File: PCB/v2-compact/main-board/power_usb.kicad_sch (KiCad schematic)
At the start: 0 parts

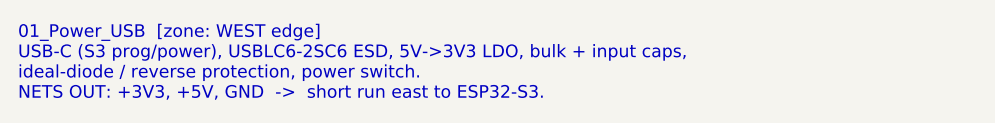
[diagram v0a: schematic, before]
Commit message: PCB: rework main board to phone-style layout; J1 -> horizontal strip
Main board (per feedback) is now a phone-style split — front is pure UI, back
carries the electronics:
- FRONT: status LEDs at the very top (above the display), TFT rotated to
  LANDSCAPE (sideways), nav buttons below it and moved down. Same feel as the
  ESP32-DIV, sideways screen.
- BACK: ESP32-S3 behind the display, microSD beside it, power + USB-C at the
  bottom-centre edge like a phone.

To keep the centre column free for the landscape display and the bottom-centre
USB-C, J1 is reoriented from a vertical 2x10 to a HORIZONTAL 10x2 strip in the
lower-centre. J1 is the shared mating datum, so the shield's J1 moves to match;
the shield's RV1106 / HTRC110 / bulk-cap zones shift to sit above/below the new
strip (SPI spine still runs north from it). Every v1 capability unchanged.

Updated both .kicad_pcb, both floorplan SVGs, both schematics' zone specs, and
PLACEMENT.md. Verified: files parse, J1 clears all zones, no same-side overlaps.

Co-Authored-By: Claude <noreply@anthropic.com>
Claude-Session: https://claude.ai/code/session_017BEAKBRVwbUCc7Sa2o3Ye7
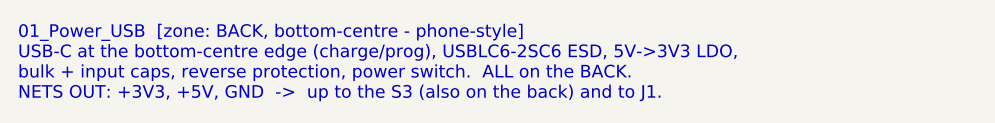
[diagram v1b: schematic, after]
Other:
- note added: "01_Power_USB [zone: BACK, bottom-centre - phone-style] USB-C at the bottom-centre edge (charge/prog), USBLC6-2SC6 ESD, 5V->3V3 LDO, bulk + input caps, reverse protection, power switch. ALL on the BACK. NETS OUT: +3V3, +5V, GND -> up to the S3 (also on the back) and to J1."
- note removed: "01_Power_USB [zone: WEST edge] USB-C (S3 prog/power), USBLC6-2SC6 ESD, 5V->3V3 LDO, bulk + input caps, ideal-diode / reverse protection, power switch. NETS OUT: +3V3, +5V, GND -> short run east to ESP32-S3."
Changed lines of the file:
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@@
   (paper "A4")
   (title_block (title "01_Power_USB") (company "YurilLAB"))
-  (text "01_Power_USB  [zone: WEST edge]
-USB-C (S3 prog/power), USBLC6-2SC6 ESD, 5V->3V3 LDO, bulk + input caps,
-ideal-diode / reverse protection, power switch.
-NETS OUT: +3V3, +5V, GND  ->  short run east to ESP32-S3." (at 15 15 0)
+  (text "01_Power_USB  [zone: BACK, bottom-centre - phone-style]
+USB-C at the bottom-centre edge (charge/prog), USBLC6-2SC6 ESD, 5V->3V3 LDO,
+bulk + input caps, reverse protection, power switch.  ALL on the BACK.
+NETS OUT: +3V3, +5V, GND  ->  up to the S3 (also on the back) and to J1." (at 15 15 0)
     (effects (font (size 1.4 1.4)) (justify left top)))
   (sheet_instances (path "/" (page "1")))
